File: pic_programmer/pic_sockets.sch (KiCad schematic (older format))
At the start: 9 parts, among them P2 SUPP28, P3 SUPP40, U1 24Cxx, U5 PIC_18_PINS, U6 PIC_8_PINS

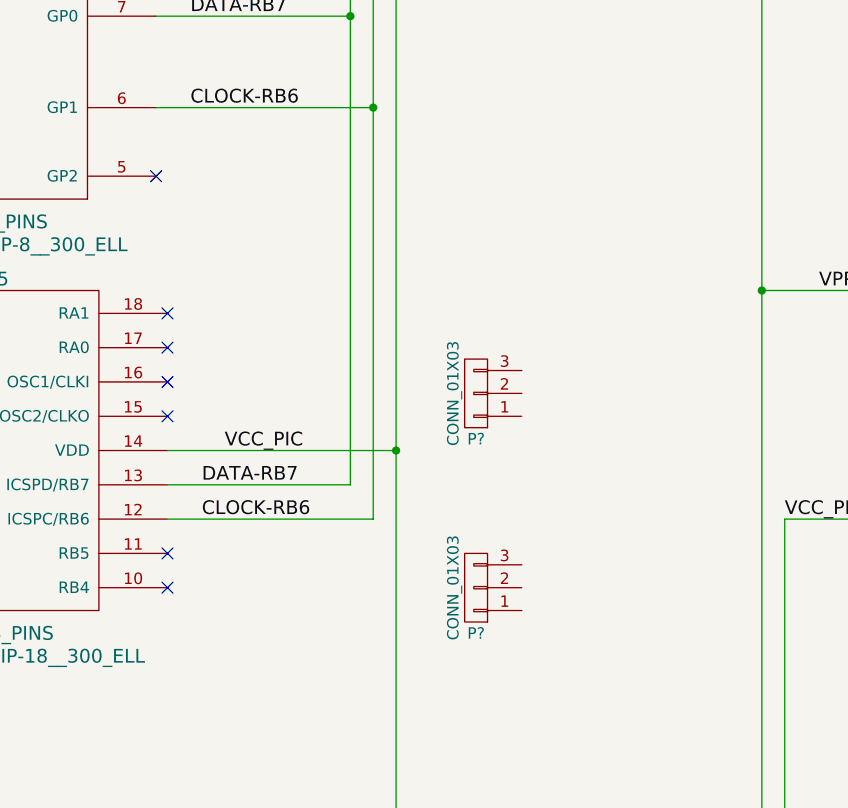
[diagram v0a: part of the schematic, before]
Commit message: added bus lines
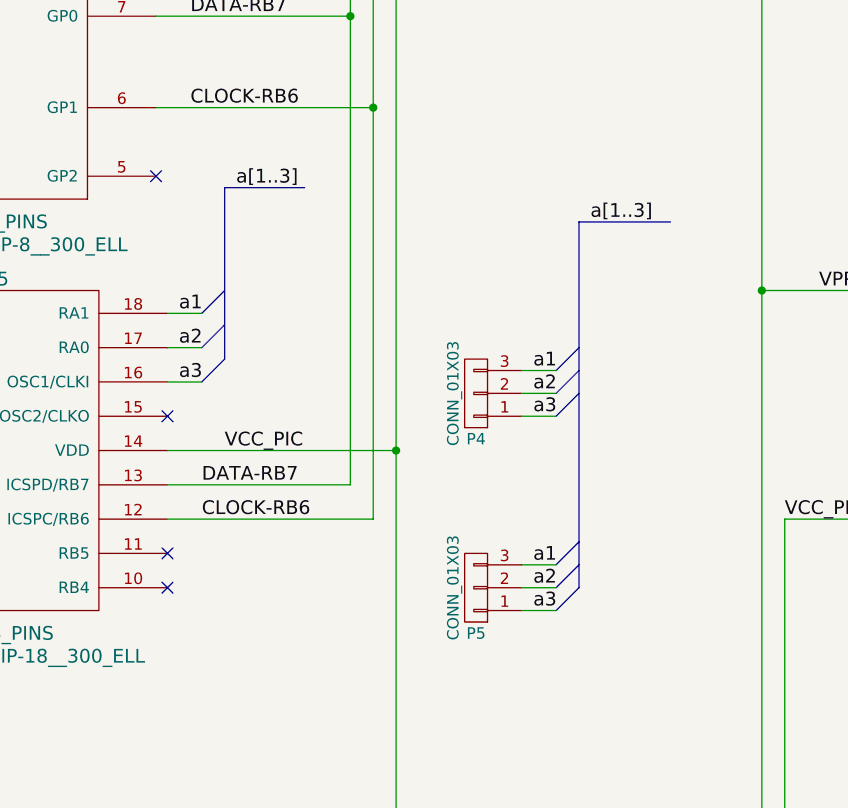
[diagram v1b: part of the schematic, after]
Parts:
- gave numbers to parts that had none: 2
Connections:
- net labels added: a1, a2, a3, a[1..3]
- wire segments 46 -> 55
- no-connect marks 71 -> 68
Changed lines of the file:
@@
 NoConn ~ 4500 5200
 NoConn ~ 4500 5050
-NoConn ~ 4500 4300
 NoConn ~ 4500 4450
-NoConn ~ 4500 4150
-NoConn ~ 4500 4000
 NoConn ~ 2950 5200
 NoConn ~ 2950 5050
@@
 $EndComp
 $Comp
-L CONN_01X03 P?
+L CONN_01X03 P5
 U 1 1 5CF168BA
 P 5850 5200
-F 0 "P?" H 5850 5400 50  0000 C CNN
+F 0 "P5" H 5850 5400 50  0000 C CNN
 F 1 "CONN_01X03" V 5950 5200 50  0000 C CNN
 F 2 "" H 5850 5200 50  0000 C CNN
@@
 $EndComp
 $Comp
-L CONN_01X03 P?
+L CONN_01X03 P4
 U 1 1 5CF168F5
 P 5850 4350
-F 0 "P?" H 5850 4550 50  0000 C CNN
+F 0 "P4" H 5850 4550 50  0000 C CNN
 F 1 "CONN_01X03" V 5950 4350 50  0000 C CNN
 F 2 "" H 5850 4350 50  0000 C CNN
@@
 	-1   0    0    1
 $EndComp
+Wire Wire Line
+	4500 4000 4650 4000
+Wire Wire Line
+	4500 4150 4650 4150
+Wire Wire Line
+	4500 4300 4650 4300
+Wire Wire Line
+	6050 4250 6200 4250
+Wire Wire Line
+	6050 4350 6200 4350
+Wire Wire Line
+	6050 4450 6200 4450
+Wire Wire Line
+	6050 5100 6200 5100
+Wire Wire Line
+	6050 5200 6200 5200
+Wire Wire Line
+	6050 5300 6200 5300
+Entry Bus Bus
+	4650 4000 4750 3900
+Entry Bus Bus
+	4650 4150 4750 4050
+Entry Bus Bus
+	4650 4300 4750 4200
+Entry Bus Bus
+	6200 4250 6300 4150
+Entry Bus Bus
+	6200 4350 6300 4250
+Entry Bus Bus
+	6200 4450 6300 4350
+Entry Bus Bus
+	6200 5100 6300 5000
+Entry Bus Bus
+	6200 5200 6300 5100
+Entry Bus Bus
+	6200 5300 6300 5200
+Wire Bus Line
+	4750 3450 4750 4200
+Wire Bus Line
+	4750 3450 5100 3450
+Wire Bus Line
+	6300 3600 6300 5200
+Wire Bus Line
+	6300 3600 6700 3600
+Text Label 4550 4000 0    60   ~ 0
+a1
+Text Label 4550 4150 0    60   ~ 0
+a2
+Text Label 4550 4300 0    60   ~ 0
+a3
+Text Label 6100 4250 0    60   ~ 0
+a1
+Text Label 6100 4350 0    60   ~ 0
+a2
+Text Label 6100 4450 0    60   ~ 0
+a3
+Text Label 6100 5100 0    60   ~ 0
+a1
+Text Label 6100 5200 0    60   ~ 0
+a2
+Text Label 6100 5300 0    60   ~ 0
+a3
+Text Label 4800 3450 0    60   ~ 0
+a[1..3]
+Text Label 6350 3600 0    60   ~ 0
+a[1..3]
 $EndSCHEMATC

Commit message: associated netlist with footprint in cvpcb for 2 sockets.
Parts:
- P4: footprint (none) -> Sockets_MOLEX_KK-System:Socket_MOLEX-KK-RM2-54mm_Lock_3pin_straight
- P5: footprint (none) -> Sockets_MOLEX_KK-System:Socket_MOLEX-KK-RM3-96mm_Lock_3pin_straight
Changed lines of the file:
@@
 F 0 "P5" H 5850 5400 50  0000 C CNN
 F 1 "CONN_01X03" V 5950 5200 50  0000 C CNN
-F 2 "" H 5850 5200 50  0000 C CNN
+F 2 "Sockets_MOLEX_KK-System:Socket_MOLEX-KK-RM3-96mm_Lock_3pin_straight" H 5850 5200 50  0001 C CNN
 F 3 "" H 5850 5200 50  0000 C CNN
 	1    5850 5200
@@
 F 0 "P4" H 5850 4550 50  0000 C CNN
 F 1 "CONN_01X03" V 5950 4350 50  0000 C CNN
-F 2 "" H 5850 4350 50  0000 C CNN
+F 2 "Sockets_MOLEX_KK-System:Socket_MOLEX-KK-RM2-54mm_Lock_3pin_straight" H 5850 4350 50  0001 C CNN
 F 3 "" H 5850 4350 50  0000 C CNN
 	1    5850 4350
